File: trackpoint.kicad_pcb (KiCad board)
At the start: 2 copper layers, 27.5 x 35 mm, 32 parts, among them P1 CONN_10, P2 CONN_5, P3 CONN_8, U1 MKL03Z32VFK4, U4 ESD

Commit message: Disconnect pin 5 of the pogo pin connector.
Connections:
- P2 pad 5: GND -> Net-(P2-Pad5)
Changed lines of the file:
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@@
     (zones 0)
     (modules 32)
-    (nets 37)
+    (nets 38)
   )
   (page A3)
@@
   (net 35 "Net-(U1-Pad5)")
   (net 36 "Net-(U1-Pad14)")
+  (net 37 "Net-(P2-Pad5)")
   (net_class Default "This is the default net class."
     (clearance 0.2032)
@@
     (add_net "Net-(P1-Pad5)")
     (add_net "Net-(P1-Pad6)")
+    (add_net "Net-(P2-Pad5)")
     (add_net "Net-(P3-Pad1)")
     (add_net "Net-(P3-Pad2)")
@@
       (net 4 GND) (clearance 0.0762))
     (pad 5 thru_hole roundrect (at -2.75 6.8) (size 2 1.2) (drill 0.7) (layers *.Cu *.Mask) (roundrect_rratio 0.25)
-      (net 4 GND) (clearance 0.0762))
+      (net 37 "Net-(P2-Pad5)") (clearance 0.0762))
     (pad "" np_thru_hole circle (at -2.5 -5.1) (size 1.6 1.6) (drill 1.6) (layers *.Cu *.Mask)
       (clearance 0.00254))

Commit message: Update Kailh microswitches.
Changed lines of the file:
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@@
     (add_net "Net-(VR1-Pad4)")
+  )
+  (module ugl:CMI126603D08 locked (layer F.Cu)
+    (at 212.660004 144.268997 180)
+    (fp_text reference SW_R1 (at -3.739996 3.468997) (layer F.SilkS)
+      (effects (font (size 0.75 0.75) (thickness 0.15)))
+    )
+    (fp_text value CMI126603D08 (at 2.060004 -2.231003) (layer F.SilkS)
+      (effects (font (size 0.75 0.75) (thickness 0.15)))
+    )
+    (fp_line (start -3.5 1.5) (end -3.5 -1.5) (layer F.SilkS) (width 0.2))
+    (fp_line (start -2 1.5) (end -3.5 1.5) (layer F.SilkS) (width 0.2))
+    (fp_line (start -2 -1.5) (end -2 1.5) (layer F.SilkS) (width 0.2))
+    (fp_line (start -3.5 -1.5) (end -2 -1.5) (layer F.SilkS) (width 0.2))
+    (fp_line (start 6.4 -2.9) (end 6.4 2.9) (layer F.SilkS) (width 0.2))
+    (fp_line (start -6.4 2.9) (end 6.4 2.9) (layer F.SilkS) (width 0.2))
+    (fp_line (start -6.4 -2.9) (end -6.4 2.9) (layer F.SilkS) (width 0.2))
+    (fp_line (start 6.4 -2.9) (end -6.4 -2.9) (layer F.SilkS) (width 0.2))
+    (pad "" thru_hole circle (at 5.08 0 180) (size 2.2 2.2) (drill 1.2) (layers *.Cu *.Mask))
+    (pad 2 thru_hole circle (at 0 0 180) (size 2.2 2.2) (drill 1.2) (layers *.Cu *.Mask)
+      (net 4 GND))
+    (pad 1 thru_hole circle (at -5.08 0 180) (size 2.2 2.2) (drill 1.2) (layers *.Cu *.Mask)
+      (net 27 /KEY_MRIGHT))
+  )
+  (module ugl:CMI126603D08 locked (layer F.Cu)
+    (at 199.360001 144.268997)
+    (fp_text reference SW_L1 (at -1.560001 -3.568997) (layer F.SilkS)
+      (effects (font (size 0.75 0.75) (thickness 0.15)))
+    )
+    (fp_text value CMI126603D08 (at 2.039999 2.231003) (layer F.SilkS)
+      (effects (font (size 0.75 0.75) (thickness 0.15)))
+    )
+    (fp_line (start -3.5 1.5) (end -3.5 -1.5) (layer F.SilkS) (width 0.2))
+    (fp_line (start -2 1.5) (end -3.5 1.5) (layer F.SilkS) (width 0.2))
+    (fp_line (start -2 -1.5) (end -2 1.5) (layer F.SilkS) (width 0.2))
+    (fp_line (start -3.5 -1.5) (end -2 -1.5) (layer F.SilkS) (width 0.2))
+    (fp_line (start 6.4 -2.9) (end 6.4 2.9) (layer F.SilkS) (width 0.2))
+    (fp_line (start -6.4 2.9) (end 6.4 2.9) (layer F.SilkS) (width 0.2))
+    (fp_line (start -6.4 -2.9) (end -6.4 2.9) (layer F.SilkS) (width 0.2))
+    (fp_line (start 6.4 -2.9) (end -6.4 -2.9) (layer F.SilkS) (width 0.2))
+    (pad "" thru_hole circle (at 5.08 0) (size 2.2 2.2) (drill 1.2) (layers *.Cu *.Mask))
+    (pad 2 thru_hole circle (at 0 0) (size 2.2 2.2) (drill 1.2) (layers *.Cu *.Mask)
+      (net 4 GND))
+    (pad 1 thru_hole circle (at -5.08 0) (size 2.2 2.2) (drill 1.2) (layers *.Cu *.Mask)
+      (net 29 /KEY_MLEFT))
   )
   (module ugl:SM0603_Diode (layer F.Cu)
@@
     )
   )
-  (module ugl:CMI126603D08 locked (layer F.Cu)
-    (at 212.660004 144.268997 180)
-    (fp_text reference SW_R1 (at -3.739996 3.468997) (layer F.SilkS)
-      (effects (font (size 0.75 0.75) (thickness 0.15)))
-    )
-    (fp_text value CMI126603D08 (at 2.060004 -2.231003) (layer F.SilkS)
-      (effects (font (size 0.75 0.75) (thickness 0.15)))
-    )
-    (fp_line (start -3.5 1.5) (end -3.5 -1.5) (layer F.SilkS) (width 0.2))
-    (fp_line (start -2 1.5) (end -3.5 1.5) (layer F.SilkS) (width 0.2))
-    (fp_line (start -2 -1.5) (end -2 1.5) (layer F.SilkS) (width 0.2))
-    (fp_line (start -3.5 -1.5) (end -2 -1.5) (layer F.SilkS) (width 0.2))
-    (fp_line (start 6.4 -2.9) (end 6.4 2.9) (layer F.SilkS) (width 0.2))
-    (fp_line (start -6.4 2.9) (end 6.4 2.9) (layer F.SilkS) (width 0.2))
-    (fp_line (start -6.4 -2.9) (end -6.4 2.9) (layer F.SilkS) (width 0.2))
-    (fp_line (start 6.4 -2.9) (end -6.4 -2.9) (layer F.SilkS) (width 0.2))
-    (pad "" np_thru_hole circle (at 5.08 0 180) (size 1.2 1.2) (drill 1.2) (layers *.Cu *.Mask))
-    (pad 2 thru_hole circle (at 0 0 180) (size 2.2 2.2) (drill 1.2) (layers *.Cu *.Mask)
-      (net 4 GND))
-    (pad 1 thru_hole circle (at -5.08 0 180) (size 2.2 2.2) (drill 1.2) (layers *.Cu *.Mask)
-      (net 27 /KEY_MRIGHT))
-  )
-  (module ugl:CMI126603D08 locked (layer F.Cu)
-    (at 199.360001 144.268997)
-    (fp_text reference SW_L1 (at -1.560001 -3.568997) (layer F.SilkS)
-      (effects (font (size 0.75 0.75) (thickness 0.15)))
-    )
-    (fp_text value CMI126603D08 (at 2.039999 2.231003) (layer F.SilkS)
-      (effects (font (size 0.75 0.75) (thickness 0.15)))
-    )
-    (fp_line (start -3.5 1.5) (end -3.5 -1.5) (layer F.SilkS) (width 0.2))
-    (fp_line (start -2 1.5) (end -3.5 1.5) (layer F.SilkS) (width 0.2))
-    (fp_line (start -2 -1.5) (end -2 1.5) (layer F.SilkS) (width 0.2))
-    (fp_line (start -3.5 -1.5) (end -2 -1.5) (layer F.SilkS) (width 0.2))
-    (fp_line (start 6.4 -2.9) (end 6.4 2.9) (layer F.SilkS) (width 0.2))
-    (fp_line (start -6.4 2.9) (end 6.4 2.9) (layer F.SilkS) (width 0.2))
-    (fp_line (start -6.4 -2.9) (end -6.4 2.9) (layer F.SilkS) (width 0.2))
-    (fp_line (start 6.4 -2.9) (end -6.4 -2.9) (layer F.SilkS) (width 0.2))
-    (pad "" np_thru_hole circle (at 5.08 0) (size 1.2 1.2) (drill 1.2) (layers *.Cu *.Mask))
-    (pad 2 thru_hole circle (at 0 0) (size 2.2 2.2) (drill 1.2) (layers *.Cu *.Mask)
-      (net 4 GND))
-    (pad 1 thru_hole circle (at -5.08 0) (size 2.2 2.2) (drill 1.2) (layers *.Cu *.Mask)
-      (net 29 /KEY_MLEFT))
-  )
   (module ugl:hole_2.9mm locked (layer F.Cu)

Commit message: Replace resistors from 4.7K to 5.1K and from 47 to 33 ohms.
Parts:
- R1: value 4.7K -> 5.1K
- R6, R7: value 47 -> 33
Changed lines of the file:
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@@
-(kicad_pcb (version 20171130) (host pcbnew 5.1.5-52549c5~84~ubuntu18.04.1)
+(kicad_pcb (version 20171130) (host pcbnew 5.1.5-52549c5~86~ubuntu18.04.1)
   (general
     (thickness 1.6)
@@
       (effects (font (size 0.75 0.75) (thickness 0.15)))
     )
-    (fp_text value 47 (at -2.7 1.6 90) (layer F.SilkS)
+    (fp_text value 33 (at -2.7 1.6 90) (layer F.SilkS)
       (effects (font (size 0.75 0.75) (thickness 0.15)))
     )
@@
       (effects (font (size 0.75 0.75) (thickness 0.15)))
     )
-    (fp_text value 47 (at -2.7 0.7 90) (layer F.SilkS)
+    (fp_text value 33 (at -2.7 0.7 90) (layer F.SilkS)
       (effects (font (size 0.75 0.75) (thickness 0.15)))
     )
@@
       (effects (font (size 0.75 0.75) (thickness 0.15)))
     )
-    (fp_text value 4.7K (at 0 1.1 270) (layer F.SilkS)
-      (effects (font (size 0.75 0.75) (thickness 0.15)))
-    )
+    (fp_text value 5.1K (at 0 1.1 270) (layer F.SilkS)
+      (effects (font (size 0.75 0.75) (thickness 0.15)))
+    )

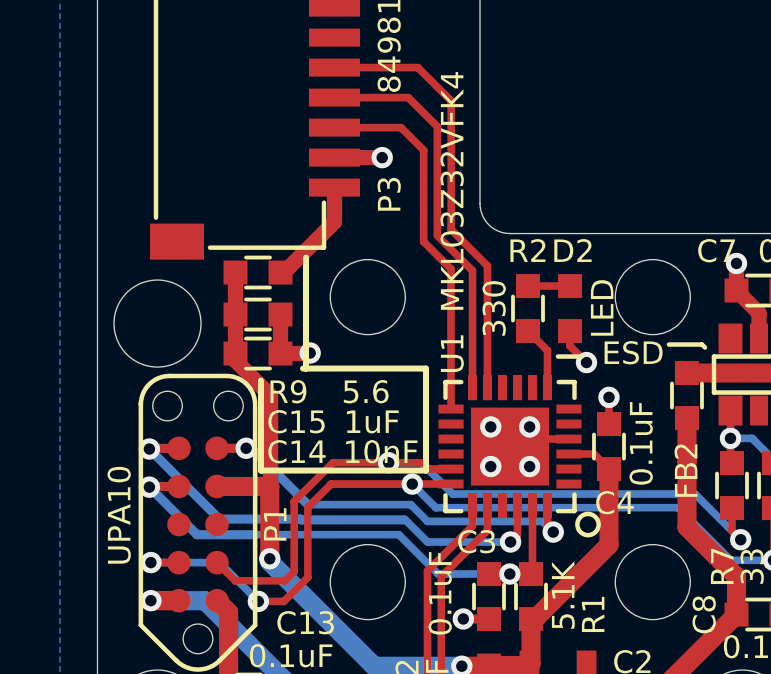
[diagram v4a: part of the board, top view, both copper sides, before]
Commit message: Remove redundant R9, C14, and C15.
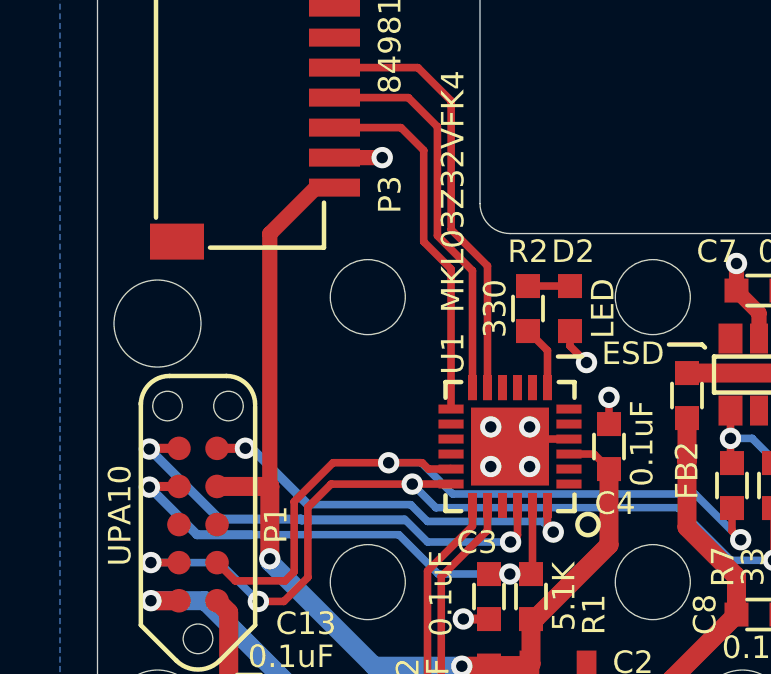
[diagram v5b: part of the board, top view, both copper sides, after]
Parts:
- removed C14: 10nF, ugl:SM0603
- removed C15: 1uF, ugl:SM0603
- removed R9: 5.6, ugl:SM0603
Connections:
- P3 pad 8: Net-(P3-Pad8) -> +3V3
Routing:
- net Net-(P3-Pad8): track 3.64 -> 0.00 mm
- net +3V3: track 31.3 -> 34.2 mm
- net GND: track 23.4 -> 21.1 mm, vias 12 -> 11

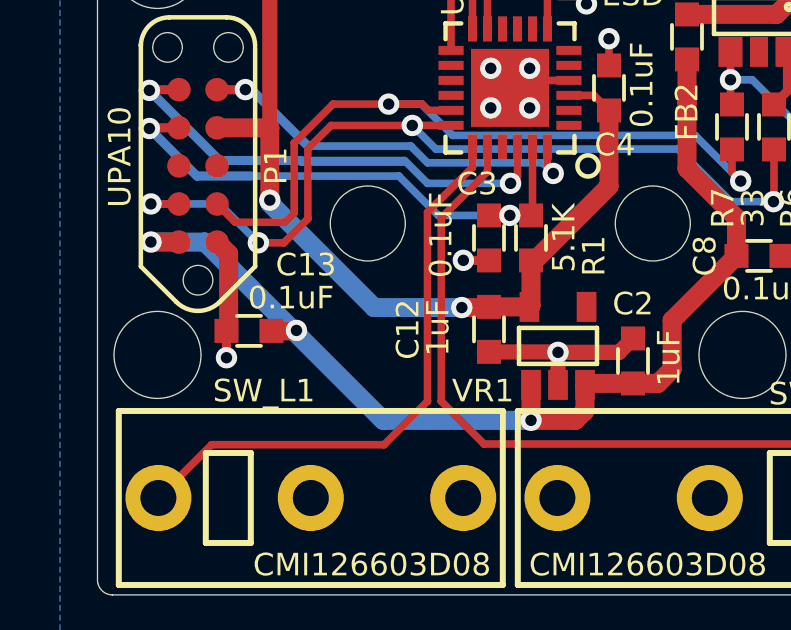
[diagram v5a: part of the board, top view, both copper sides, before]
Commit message: Remove redundant C13.
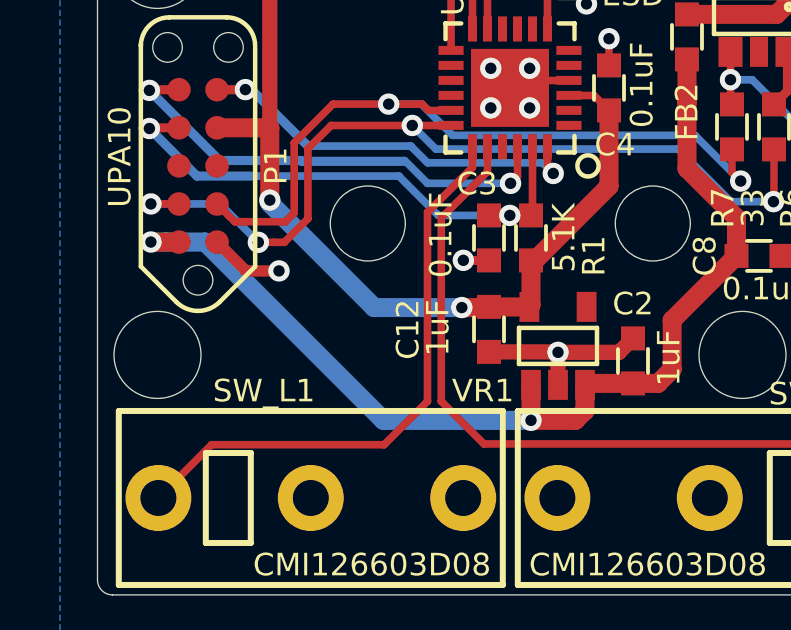
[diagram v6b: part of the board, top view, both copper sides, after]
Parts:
- removed C13: 0.1uF, ugl:SM0603
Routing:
- net GND: track 21.1 -> 19.5 mm
- net +5V: track 36.3 -> 35.5 mm, vias 3 -> 2
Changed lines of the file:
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@@
     (thickness 1.6)
     (drawings 24)
-    (tracks 213)
+    (tracks 212)
     (zones 0)
-    (modules 29)
+    (modules 28)
     (nets 37)
   )
@@
   )
   (setup
-    (last_trace_width 0.508)
+    (last_trace_width 0.381)
     (user_trace_width 0.254)
     (user_trace_width 0.3048)
@@
   )
   (module ugl:SM0603 (layer F.Cu)
-    (at 197.3 138.7)
-    (attr smd)
-    (fp_text reference C13 (at 1.9 -2.2) (layer F.SilkS)
-      (effects (font (size 0.75 0.75) (thickness 0.15)))
-    )
-    (fp_text value 0.1uF (at 1.4 -1.1) (layer F.SilkS)
-      (effects (font (size 0.75 0.75) (thickness 0.15)))
-    )
-    (fp_line (start 0.4 0.5) (end -0.4 0.5) (layer F.SilkS) (width 0.127))
-    (fp_line (start -0.4 -0.5) (end 0.4 -0.5) (layer F.SilkS) (width 0.127))
-    (pad 2 smd rect (at 0.75 0) (size 0.8 0.8) (layers F.Cu F.Paste F.Mask)
-      (net 8 +5V))
-    (pad 1 smd rect (at -0.75 0) (size 0.8 0.8) (layers F.Cu F.Paste F.Mask)
-      (net 4 GND))
-    (model smd\resistors\R0603.wrl
-      (offset (xyz 0 0 0.02540000082496551))
-      (scale (xyz 0.5 0.5 0.5))
-      (rotate (xyz 0 0 0))
-    )
-  )
-  (module ugl:SM0603 (layer F.Cu)
     (at 211.9 128.9 270)
     (attr smd)
@@
   (segment (start 215.05 136.2) (end 216.999997 136.2) (width 0.381) (layer F.Cu) (net 4))
   (via (at 208.55 127.8) (size 0.7112) (drill 0.381) (layers F.Cu B.Cu) (net 4))
-  (segment (start 196.55 138.7) (end 196.55 139.5936) (width 0.3048) (layer F.Cu) (net 4))
-  (via (at 196.55 139.5936) (size 0.7112) (drill 0.381) (layers F.Cu B.Cu) (net 4))
-  (segment (start 196.6214 136.1264) (end 196.6214 138.6586) (width 0.635) (layer F.Cu) (net 4))
-  (segment (start 196.235 135.74) (end 196.6214 136.1264) (width 0.635) (layer F.Cu) (net 4))
   (segment (start 208 126.75) (end 208 127.25) (width 0.254) (layer F.Cu) (net 4))
   (segment (start 208 127.25) (end 208.55 127.8) (width 0.254) (layer F.Cu) (net 4))
+  (via (at 198.299994 136.7) (size 0.7112) (drill 0.381) (layers F.Cu B.Cu) (net 4))
+  (segment (start 198.299994 136.7) (end 197.2 136.7) (width 0.381) (layer F.Cu) (net 4))
+  (segment (start 197.2 136.7) (end 196.3 135.8) (width 0.381) (layer F.Cu) (net 4))
   (segment (start 206.75 134.8) (end 206.7 134.85) (width 0.254) (layer F.Cu) (net 5))
   (segment (start 206.75 132.565) (end 206.75 134.8) (width 0.254) (layer F.Cu) (net 5))
@@
   (segment (start 201.9554 131.1402) (end 201.9554 131.1402) (width 0.254) (layer B.Cu) (net 6))
   (via (at 201.9554 131.1402) (size 0.7112) (drill 0.381) (layers F.Cu B.Cu) (net 6))
-  (segment (start 201.9554 131.1402) (end 200.1012 131.1402) (width 0.254) (layer F.Cu) (net 6))
-  (segment (start 200.1012 131.1402) (end 198.8058 132.4356) (width 0.254) (layer F.Cu) (net 6))
-  (segment (start 198.8058 132.4356) (end 198.8058 134.7724) (width 0.254) (layer F.Cu) (net 6))
-  (segment (start 198.8058 134.7724) (end 198.501 135.0772) (width 0.254) (layer F.Cu) (net 6))
-  (segment (start 196.8422 135.0772) (end 196.235 134.47) (width 0.254) (layer F.Cu) (net 6))
-  (segment (start 198.501 135.0772) (end 196.8422 135.0772) (width 0.254) (layer F.Cu) (net 6))
   (segment (start 204.035 131.35) (end 203.2828 131.35) (width 0.254) (layer F.Cu) (net 6))
   (segment (start 203.073 131.1402) (end 201.9554 131.1402) (width 0.254) (layer F.Cu) (net 6))
   (segment (start 203.2828 131.35) (end 203.073 131.1402) (width 0.254) (layer F.Cu) (net 6))
+  (segment (start 196.826588 135.061588) (end 196.627429 134.862429) (width 0.254) (layer F.Cu) (net 6))
+  (segment (start 196.627429 134.862429) (end 196.235 134.47) (width 0.254) (layer F.Cu) (net 6))
+  (segment (start 198.8058 132.4356) (end 198.8058 134.7724) (width 0.254) (layer F.Cu) (net 6))
+  (segment (start 201.9554 131.1402) (end 200.1012 131.1402) (width 0.254) (layer F.Cu) (net 6))
+  (segment (start 200.1012 131.1402) (end 198.8058 132.4356) (width 0.254) (layer F.Cu) (net 6))
+  (segment (start 198.516612 135.061588) (end 196.826588 135.061588) (width 0.254) (layer F.Cu) (net 6))
+  (segment (start 198.8058 134.7724) (end 198.516612 135.061588) (width 0.254) (layer F.Cu) (net 6))
   (via (at 207.4418 133.4516) (size 0.7112) (drill 0.381) (layers F.Cu B.Cu) (net 7))
   (segment (start 207.25 132.565) (end 207.25 133.2598) (width 0.254) (layer F.Cu) (net 7))
@@
   (segment (start 194.033 135.74) (end 194.0306 135.7376) (width 0.635) (layer F.Cu) (net 8))
   (segment (start 194.965 135.74) (end 194.033 135.74) (width 0.635) (layer F.Cu) (net 8))
-  (segment (start 195.829403 135.7376) (end 194.0306 135.7376) (width 0.635) (layer B.Cu) (net 8))
-  (segment (start 206.7 141.6812) (end 201.773003 141.6812) (width 0.635) (layer B.Cu) (net 8))
-  (segment (start 201.773003 141.6812) (end 195.829403 135.7376) (width 0.635) (layer B.Cu) (net 8))
-  (segment (start 198.05 138.7) (end 198.8472 138.7) (width 0.635) (layer F.Cu) (net 8))
-  (segment (start 198.8472 138.7) (end 198.8566 138.7094) (width 0.635) (layer F.Cu) (net 8))
-  (via (at 198.882 138.684) (size 0.7112) (drill 0.381) (layers F.Cu B.Cu) (net 8))
+  (segment (start 201.784274 141.6812) (end 195.840674 135.7376) (width 0.635) (layer B.Cu) (net 8))
+  (segment (start 206.7 141.6812) (end 201.784274 141.6812) (width 0.635) (layer B.Cu) (net 8))
+  (segment (start 195.840674 135.7376) (end 194.533494 135.7376) (width 0.635) (layer B.Cu) (net 8))
+  (segment (start 194.533494 135.7376) (end 194.0306 135.7376) (width 0.635) (layer B.Cu) (net 8))
   (segment (start 206.25 132.565) (end 206.25 133.551221) (width 0.254) (layer F.Cu) (net 9))
   (via (at 206.0194 133.781821) (size 0.7112) (drill 0.381) (layers F.Cu B.Cu) (net 9))
@@
   (segment (start 202.7428 131.8514) (end 202.7174 131.826) (width 0.254) (layer B.Cu) (net 10))
   (via (at 202.7428 131.8514) (size 0.7112) (drill 0.381) (layers F.Cu B.Cu) (net 10))
-  (via (at 197.612 135.763) (size 0.7112) (drill 0.381) (layers F.Cu B.Cu) (net 10))
-  (segment (start 197.612 135.7122) (end 197.612 135.763) (width 0.254) (layer F.Cu) (net 10))
-  (segment (start 198.461792 135.763) (end 197.612 135.763) (width 0.254) (layer F.Cu) (net 10))
-  (segment (start 199.263009 134.961783) (end 198.461792 135.763) (width 0.254) (layer F.Cu) (net 10))
-  (segment (start 199.26301 132.624982) (end 199.263009 134.961783) (width 0.254) (layer F.Cu) (net 10))
-  (segment (start 202.7428 131.8514) (end 200.036592 131.8514) (width 0.254) (layer F.Cu) (net 10))
-  (segment (start 200.036592 131.8514) (end 199.26301 132.624982) (width 0.254) (layer F.Cu) (net 10))
-  (segment (start 197.612 135.763) (end 196.3166 134.4676) (width 0.254) (layer B.Cu) (net 10))
-  (segment (start 196.3166 134.4676) (end 194.0306 134.4676) (width 0.254) (layer B.Cu) (net 10))
   (via (at 194.0306 134.4676) (size 0.7112) (drill 0.381) (layers F.Cu B.Cu) (net 10))
   (segment (start 194.9626 134.4676) (end 194.965 134.47) (width 0.254) (layer F.Cu) (net 10))
@@
   (segment (start 202.7442 131.85) (end 202.7428 131.8514) (width 0.254) (layer F.Cu) (net 10))
   (segment (start 204.035 131.85) (end 202.7442 131.85) (width 0.254) (layer F.Cu) (net 10))
+  (segment (start 199.263009 134.961783) (end 198.477403 135.747389) (width 0.254) (layer F.Cu) (net 10))
+  (segment (start 197.612 135.7122) (end 197.612 135.747389) (width 0.254) (layer F.Cu) (net 10))
+  (segment (start 198.114894 135.747389) (end 197.612 135.747389) (width 0.254) (layer F.Cu) (net 10))
+  (segment (start 196.332211 134.4676) (end 197.612 135.747389) (width 0.254) (layer B.Cu) (net 10))
+  (segment (start 199.26301 132.624982) (end 199.263009 134.961783) (width 0.254) (layer F.Cu) (net 10))
+  (via (at 197.612 135.747389) (size 0.7112) (drill 0.381) (layers F.Cu B.Cu) (net 10))
+  (segment (start 194.0306 134.4676) (end 196.332211 134.4676) (width 0.254) (layer B.Cu) (net 10))
+  (segment (start 200.036592 131.8514) (end 199.26301 132.624982) (width 0.254) (layer F.Cu) (net 10))
+  (segment (start 202.7428 131.8514) (end 200.036592 131.8514) (width 0.254) (layer F.Cu) (net 10))
+  (segment (start 198.477403 135.747389) (end 198.114894 135.747389) (width 0.254) (layer F.Cu) (net 10))
   (via (at 204.3938 137.922) (size 0.7112) (drill 0.381) (layers F.Cu B.Cu) (net 12))
   (segment (start 208.8 130.85) (end 209.3 131.35) (width 0.254) (layer F.Cu) (net 12))
